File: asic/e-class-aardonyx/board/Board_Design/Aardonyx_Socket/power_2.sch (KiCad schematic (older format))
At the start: 52 parts, among them Q1 FDN339AN, SW2 FSM2JSMAATR, U10 TPS7A7002DDAR, U11 ADM1186, U13 TPS7A7002DDAR, U14 74AUP1G09GW

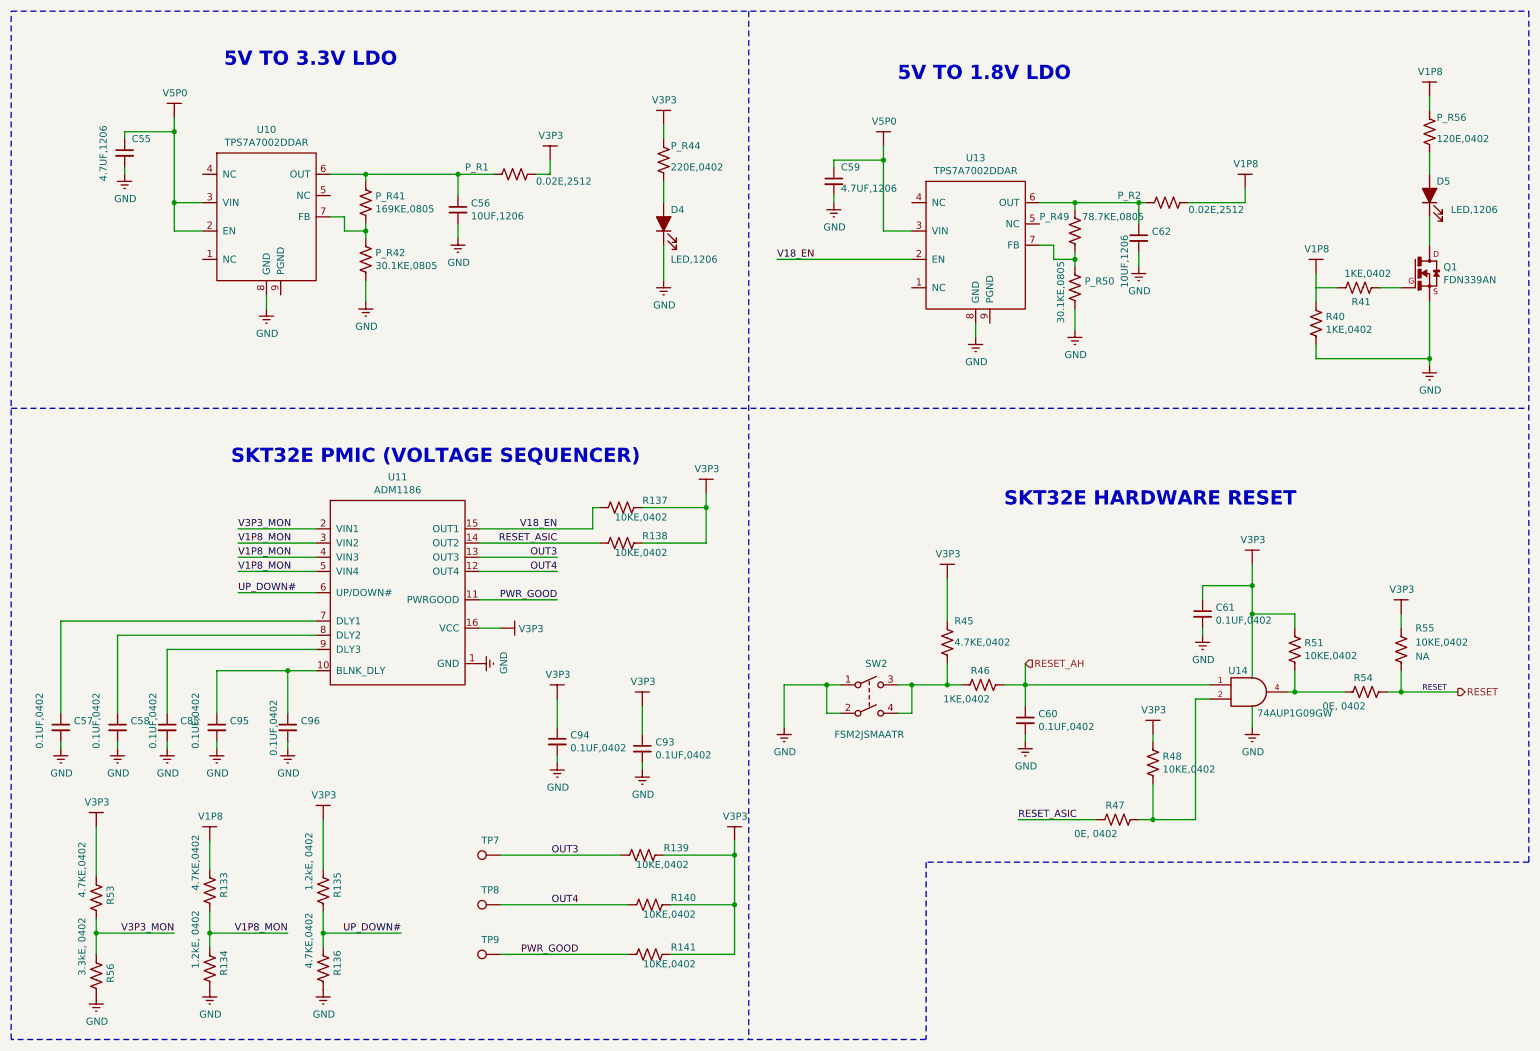
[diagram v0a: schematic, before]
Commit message: update socket compo placement
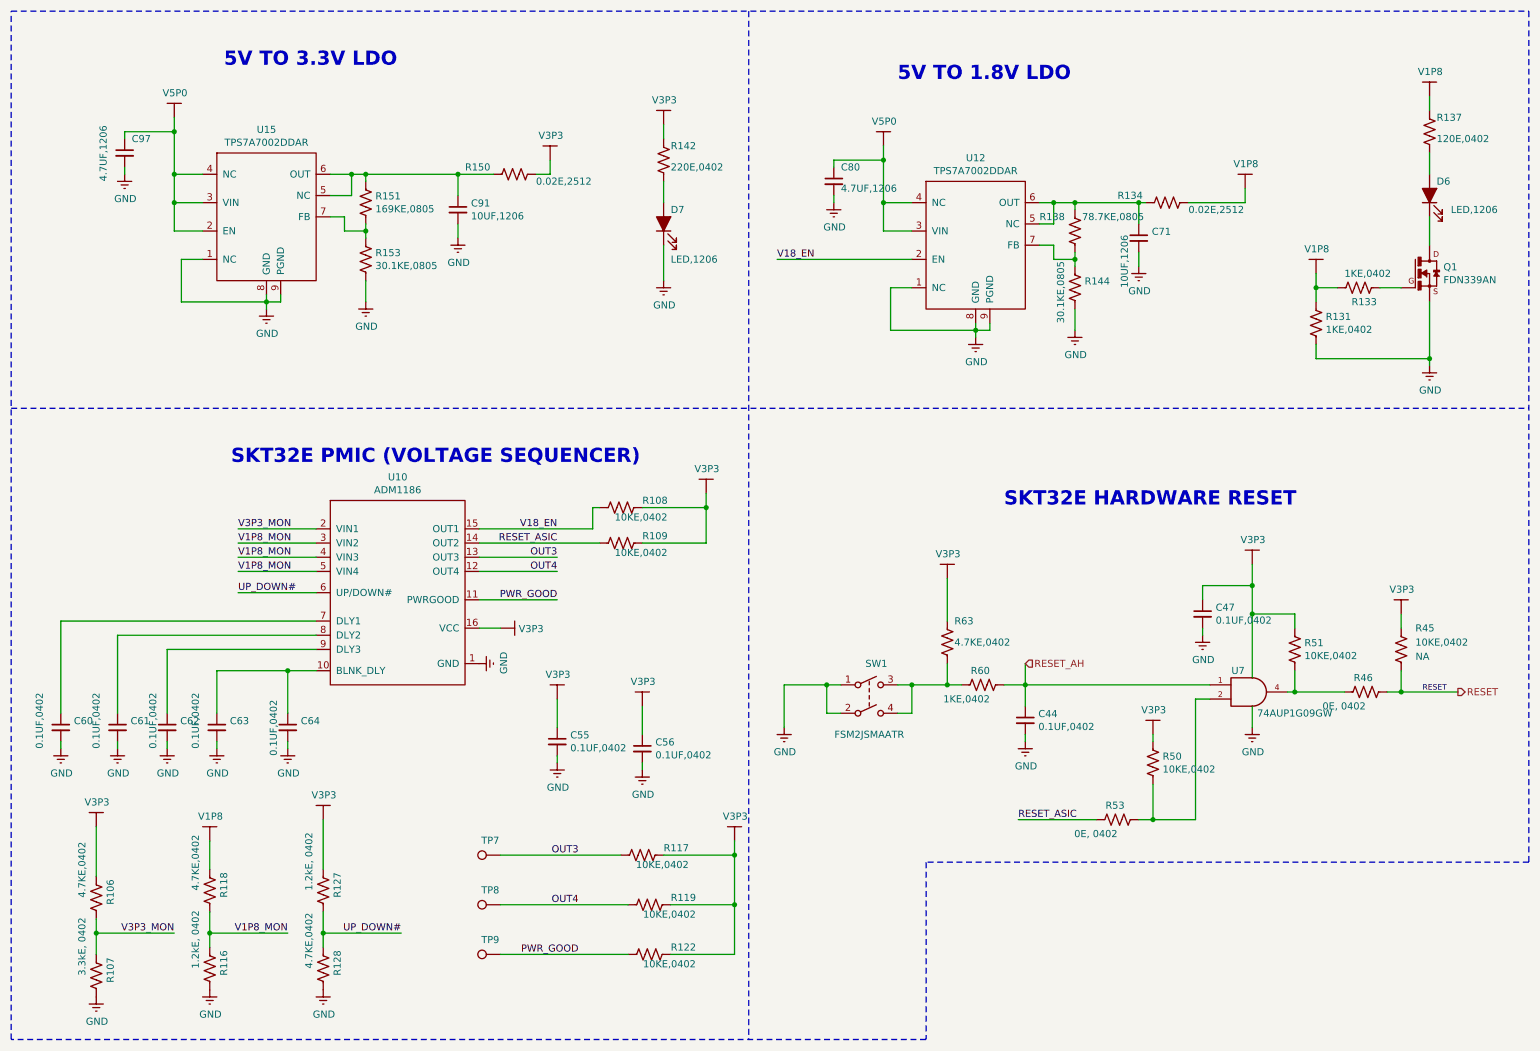
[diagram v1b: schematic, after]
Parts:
- renumbered C60 to C44, C61 to C47, C94 to C55, C93 to C56, C57 to C60, C58 to C61, C85 to C62, C95 to C63, C96 to C64, C62 to C71, C59 to C80, C56 to C91, C55 to C97, D5 to D6, D4 to D7, R53 to R106, R56 to R107, R137 to R108, R138 to R109, R134 to R116, R139 to R117, R133 to R118, R140 to R119, R141 to R122, R135 to R127, R136 to R128, R40 to R131, R41 to R133, P_R2 to R134, P_R56 to R137, P_R49 to R138, P_R44 to R142, P_R50 to R144, P_R1 to R150, P_R41 to R151, P_R42 to R153, R55 to R45, R54 to R46, R48 to R50, R47 to R53, R46 to R60, R45 to R63, SW2 to SW1, U11 to U10, U13 to U12, U10 to U15
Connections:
- net GND: now also U12.1 (NC), U12.9 (PGND), U15.1 (NC), U15.9 (PGND)
- net V5P0: now also U12.4 (NC), U15.4 (NC)
- net at C91.1, R150.2, R151.1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: now also U15.5 (NC)
- net at C71.1, R134.2, R138.1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: now also U12.5 (NC)

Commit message: Back annotation
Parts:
- renumbered C44 to C1, C47 to C2, C55 to C56, C56 to C57, C60 to C58, C61 to C59, C62 to C60, C63 to C61, C64 to C62, C71 to C69, C80 to C77, C91 to C89, C97 to C90, R60 to R10, R106 to R102, R107 to R103, R108 to R104, R109 to R105, R116 to R106, R117 to R107, R118 to R108, R119 to R109, R63 to R11, R127 to R110, R128 to R111, R122 to R112, R131 to R121, R133 to R122, R137 to R123, R134 to R126, R142 to R134, R138 to R136, R144 to R147, R150 to R148, R151 to R149, R153 to R150, R45 to R4, R46 to R5, R50 to R6, R51 to R7, R53 to R8, U15 to U14, U10 to U8, U12 to U9
